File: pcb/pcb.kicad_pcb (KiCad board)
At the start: 2 copper layers, 44.5 x 50.8 mm, 7 parts, among them SW1 SW_Push, U1 NodeMCU1.0(ESP-12E), U2 DHT22, U3 SSD1306_OLED_128x32, U4 VL6180X_Adafruit

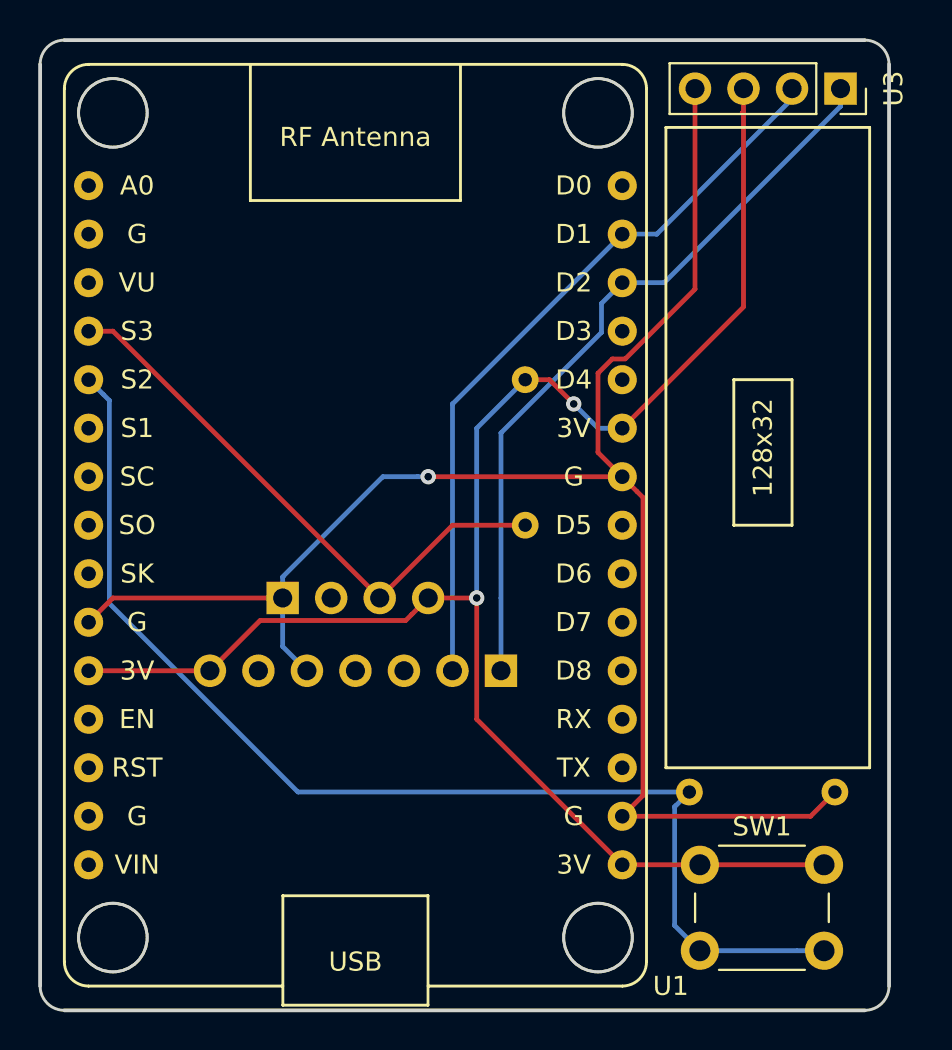
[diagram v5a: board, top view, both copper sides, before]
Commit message: Use the right ESP8266 footprint
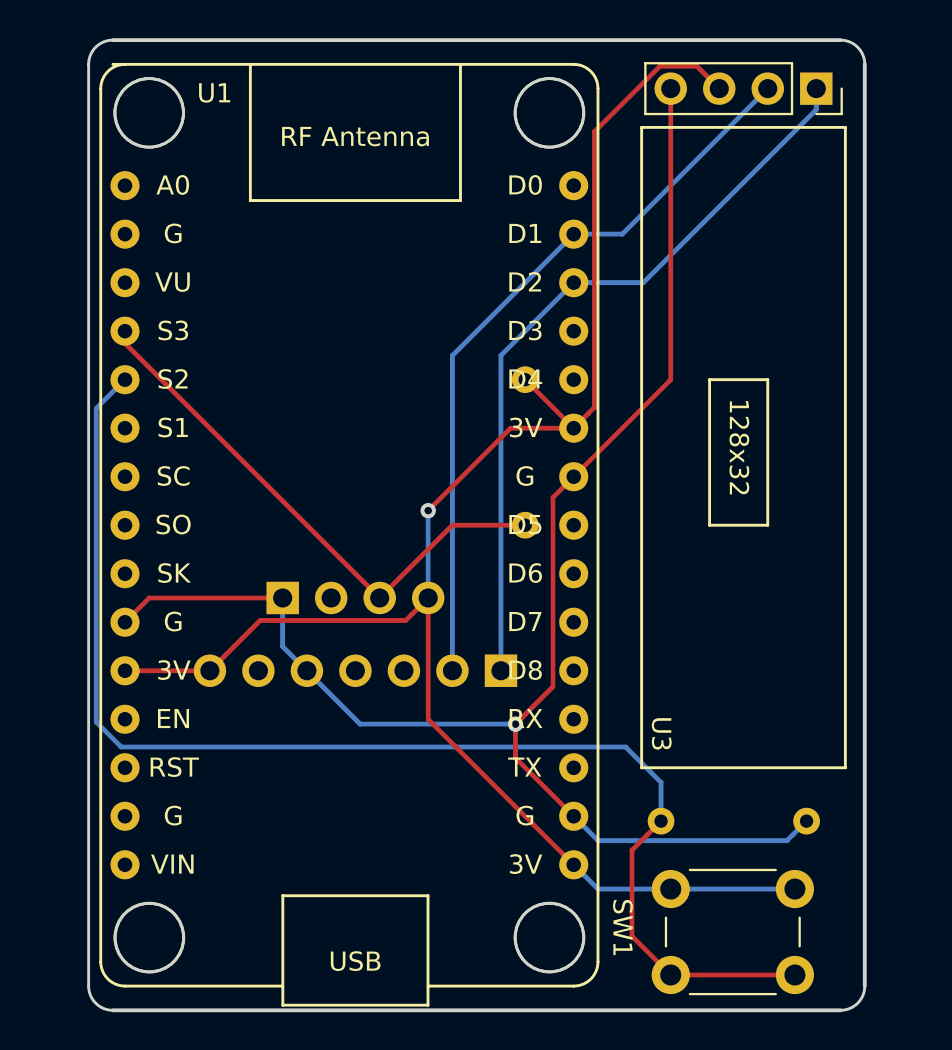
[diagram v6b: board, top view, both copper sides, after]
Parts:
- U1: footprint ESP8266:NodeMCU1.0(12-E) -> ESP8266:ESP12F-Devkit-V3
- moved R2 2.13 mm to (167.1, 115.8)
- moved SW1 1.98 mm to (167.6, 119.4)
- moved U3 1.27 mm to (175.3, 77.5)
- moved U1 1.27 mm to (151.1, 101.6)
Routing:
- net GND: track 89.8 -> 81.1 mm
- net Net-(R2-Pad1): track 62.3 -> 67.5 mm
- net Net-(R1-Pad2): track 30.2 -> 28.7 mm
- net 3v3: vias 2 -> 1
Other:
- board size 44.5 x 50.8 mm -> 40.6 x 50.8 mm
